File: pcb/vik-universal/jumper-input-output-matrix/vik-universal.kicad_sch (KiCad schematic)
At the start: 146 parts, among them J1001 Conn_01x01_Socket

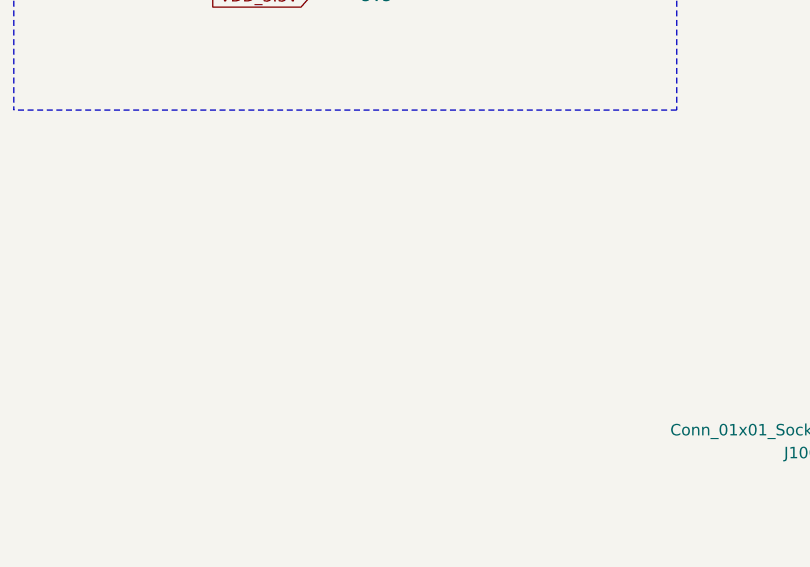
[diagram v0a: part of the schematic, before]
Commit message: vik universal jumper input output matrix - added I2C pull ups, jumpers to enable or disable I2C pull up resistors
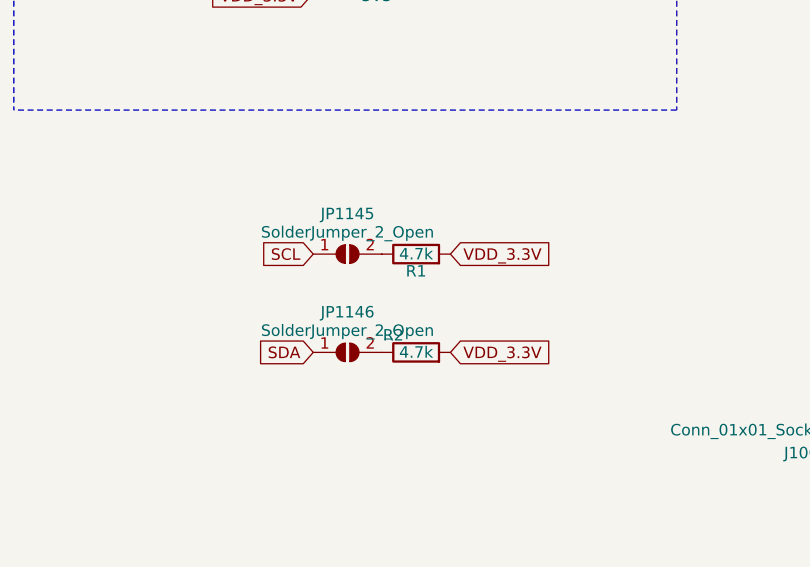
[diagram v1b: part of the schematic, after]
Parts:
- added JP1145, JP1146: SolderJumper_2_Open, Jumper:SolderJumper-2_P1.3mm_Open_RoundedPad1.0x1.5mm, symbol Jumper:SolderJumper_2_Open
- added R1, R2: 4.7k, local:D3_TH_SMD, symbol Device:R
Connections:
- net SCL: now also JP1145.1 (A)
- net SDA: now also JP1146.1 (A)
- net VDD_3.3V: now also R1.2, R2.2
- new net: JP1145.2 (B), R1.1
- new net: JP1146.2 (B), R2.1
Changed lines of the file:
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@@
+    )
+  )
+  (global_label "VDD_3.3V" (shape input) (at 63.754 115.062 0)
+    (effects (font (size 1.27 1.27)) (justify left))
+    (property "Intersheetrefs" "${INTERSHEET_REFS}" (at 74.8757 114.9826 0)
+      (effects (font (size 1.27 1.27)) (justify left) hide)
     )
   )
@@
     )
   )
+  (global_label "VDD_3.3V" (shape input) (at 63.754 125.984 0)
+    (effects (font (size 1.27 1.27)) (justify left))
+    (property "Intersheetrefs" "${INTERSHEET_REFS}" (at 74.8757 125.9046 0)
+      (effects (font (size 1.27 1.27)) (justify left) hide)
+    )
+  )
   (global_label "SCLK" (shape input) (at 50.8 58.42 180)
     (effects (font (size 1.27 1.27)) (justify right))
@@
     )
   )
+  (global_label "SCL" (shape input) (at 48.514 115.062 180)
+    (effects (font (size 1.27 1.27)) (justify right))
+    (property "Intersheetrefs" "${INTERSHEET_REFS}" (at 42.2909 115.1414 0)
+      (effects (font (size 1.27 1.27)) (justify right) hide)
+    )
+  )
   (global_label "GPIO_AD1" (shape input) (at 325.374 239.522 270)
     (effects (font (size 1.27 1.27)) (justify right))
@@
     )
   )
+  (global_label "SDA" (shape input) (at 48.514 125.984 180)
+    (effects (font (size 1.27 1.27)) (justify right))
+    (property "Intersheetrefs" "${INTERSHEET_REFS}" (at 42.2909 126.0634 0)
+      (effects (font (size 1.27 1.27)) (justify right) hide)
+    )
+  )
   (symbol (lib_id "Jumper:Jumper_2_Open") (at 383.54 53.34 270) (unit 1)
     (in_bom yes) (on_board yes) (dnp no) (fields_autoplaced)
@@
     )
   )
+  (symbol (lib_id "Jumper:SolderJumper_2_Open") (at 52.324 115.062 0) (unit 1)
+    (in_bom yes) (on_board yes) (dnp no) (fields_autoplaced)
+    (property "Reference" "JP1145" (at 52.324 110.593 0)
+      (effects (font (size 1.27 1.27)))
+    )
+    (property "Value" "SolderJumper_2_Open" (at 52.324 112.641 0)
+      (effects (font (size 1.27 1.27)))
+    )
+    (property "Footprint" "Jumper:SolderJumper-2_P1.3mm_Open_RoundedPad1.0x1.5mm" (at 52.324 115.062 0)
+      (effects (font (size 1.27 1.27)) hide)
+    )
+    (property "Datasheet" "~" (at 52.324 115.062 0)
+      (effects (font (size 1.27 1.27)) hide)
+    )
+    (pin "1")
+    (pin "2")
+    (instances
+      (project "vik-universal"
+        (path "/e63e39d7-6ac0-4ffd-8aa3-1841a4541b55"
+          (reference "JP1145") (unit 1)
+        )
+      )
+    )
+  )
   (symbol (lib_id "Jumper:Jumper_2_Open") (at 317.5 220.98 270) (unit 1)
     (in_bom yes) (on_board yes) (dnp no) (fields_autoplaced)
@@
         (path "/e63e39d7-6ac0-4ffd-8aa3-1841a4541b55"
           (reference "JP1011") (unit 1)
+        )
+      )
+    )
+  )
+  (symbol (lib_id "Device:R") (at 59.944 115.062 90) (unit 1)
+    (in_bom yes) (on_board yes) (dnp no)
+    (property "Reference" "R1" (at 59.944 116.967 90)
+      (effects (font (size 1.27 1.27)))
+    )
+    (property "Value" "4.7k" (at 59.944 115.062 90)
+      (effects (font (size 1.27 1.27)))
+    )
+    (property "Footprint" "local:D3_TH_SMD" (at 59.944 116.84 90)
+      (effects (font (size 1.27 1.27)) hide)
+    )
+    (property "Datasheet" "~" (at 59.944 115.062 0)
+      (effects (font (size 1.27 1.27)) hide)
+    )
+    (property "LCSC" "C104821" (at 59.944 115.062 90)
+      (effects (font (size 1.27 1.27)) hide)
+    )
+    (pin "1")
+    (pin "2")
+    (instances
+      (project "haptic"
+        (path "/61fe293f-6808-4b7f-9340-9aaac7054a97"
+          (reference "R1") (unit 1)
+        )
+      )
+      (project "vik-universal"
+        (path "/e63e39d7-6ac0-4ffd-8aa3-1841a4541b55"
+          (reference "R1001") (unit 1)
         )
       )
@@
     )
   )
+  (symbol (lib_id "Jumper:SolderJumper_2_Open") (at 52.324 125.984 0) (unit 1)
+    (in_bom yes) (on_board yes) (dnp no) (fields_autoplaced)
+    (property "Reference" "JP1146" (at 52.324 121.515 0)
+      (effects (font (size 1.27 1.27)))
+    )
+    (property "Value" "SolderJumper_2_Open" (at 52.324 123.563 0)
+      (effects (font (size 1.27 1.27)))
+    )
+    (property "Footprint" "Jumper:SolderJumper-2_P1.3mm_Open_RoundedPad1.0x1.5mm" (at 52.324 125.984 0)
+      (effects (font (size 1.27 1.27)) hide)
+    )
+    (property "Datasheet" "~" (at 52.324 125.984 0)
+      (effects (font (size 1.27 1.27)) hide)
+    )
+    (pin "1")
+    (pin "2")
+    (instances
+      (project "vik-universal"
+        (path "/e63e39d7-6ac0-4ffd-8aa3-1841a4541b55"
+          (reference "JP1146") (unit 1)
+        )
+      )
+    )
+  )
   (symbol (lib_id "Jumper:Jumper_2_Open") (at 284.48 220.98 270) (unit 1)
     (in_bom yes) (on_board yes) (dnp no) (fields_autoplaced)
@@
         )
       )
+    )
+  )
+  (symbol (lib_id "Device:R") (at 59.944 125.984 90) (unit 1)
+    (in_bom yes) (on_board yes) (dnp no)
+    (property "Reference" "R2" (at 57.404 124.079 90)
+      (effects (font (size 1.27 1.27)))
+    )
+    (property "Value" "4.7k" (at 59.944 125.984 90)
+      (effects (font (size 1.27 1.27)))
+    )
+    (property "Footprint" "local:D3_TH_SMD" (at 59.944 127.762 90)
+      (effects (font (size 1.27 1.27)) hide)
+    )
+    (property "Datasheet" "~" (at 59.944 125.984 0)
+      (effects (font (size 1.27 1.27)) hide)
+    )
+    (property "LCSC" "C104821" (at 59.944 125.984 90)
+      (effects (font (size 1.27 1.27)) hide)
+    )
+    (pin "1")
+    (pin "2")
+    (instances
+      (project "haptic"
+        (path "/61fe293f-6808-4b7f-9340-9aaac7054a97"
+          (reference "R2") (unit 1)
+        )
+      )
+      (project "vik-universal"
+        (path "/e63e39d7-6ac0-4ffd-8aa3-1841a4541b55"
+          (reference "R1002") (unit 1)
+        )
+      )

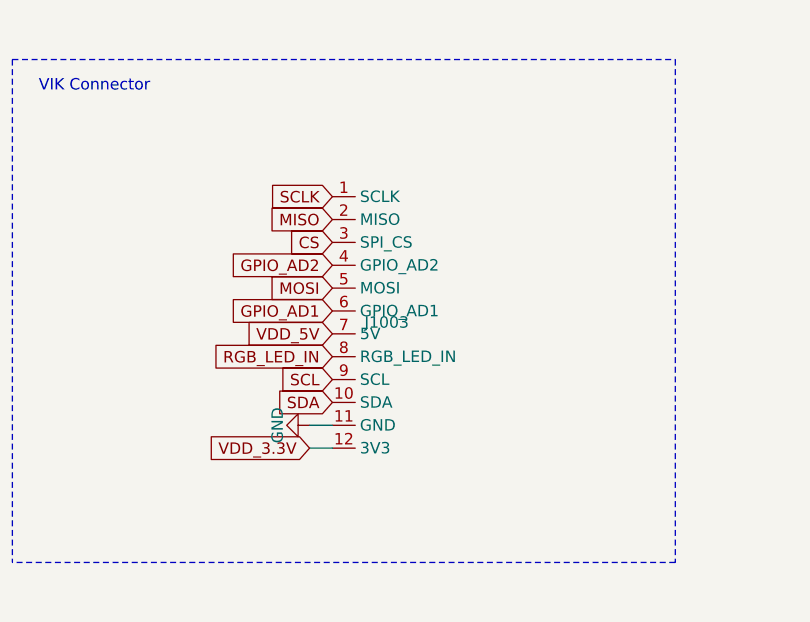
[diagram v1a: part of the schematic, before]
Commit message: updated vikm connector symbols, per some recommendations from sigprof in fingerpunch discord
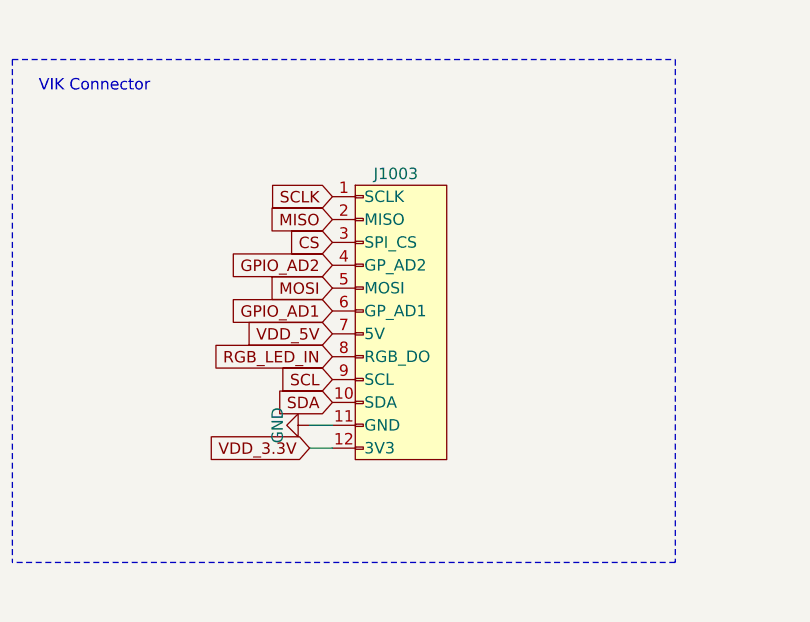
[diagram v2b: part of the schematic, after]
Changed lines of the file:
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@@
     )
   )
-  (symbol (lib_id "vik:vik-module-connector") (at 50.8 72.39 0) (unit 1)
-    (in_bom yes) (on_board yes) (dnp no) (fields_autoplaced)
-    (property "Reference" "J1003" (at 54.356 72.39 0)
+  (symbol (lib_id "vik:vik-module-connector") (at 58.42 71.12 0) (unit 1)
+    (in_bom yes) (on_board yes) (dnp no)
+    (property "Reference" "J1003" (at 55.372 55.88 0)
       (effects (font (size 1.27 1.27)) (justify left))
     )
-    (property "Value" "~" (at 50.8 66.04 0)
+    (property "Value" "~" (at 58.42 64.77 0)
       (effects (font (size 1.27 1.27)))
     )
-    (property "Footprint" "vik:vik-module-connector-horizontal" (at 50.8 66.04 0)
+    (property "Footprint" "vik:vik-module-connector-horizontal" (at 58.42 64.77 0)
       (effects (font (size 1.27 1.27)) hide)
     )
-    (property "Datasheet" "" (at 50.8 66.04 0)
+    (property "Datasheet" "" (at 58.42 64.77 0)
       (effects (font (size 1.27 1.27)) hide)
     )
-    (property "LCSC" "C2919557" (at 50.8 72.39 0)
+    (property "LCSC" "C2919557" (at 58.42 71.12 0)
       (effects (font (size 1.27 1.27)) hide)
     )
